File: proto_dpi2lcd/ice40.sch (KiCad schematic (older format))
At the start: 42 parts, among them J101 Conn_02x05_Odd_Even, J6 Conn_01x40_MountingPin, U1 ASDMB-xxxMHz, U102 iCE40HX1K-CB132, U103 W25Q32JVSS, U104 TLV71312PDBV, U105 TLV71325PDBV

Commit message: Work in progress
- Schematic of 12V to 3,3V BUCK
 - pin allocation from RPi header to FPGA
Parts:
- removed C109, C112, C113: 100n, Capacitor_SMD:C_0603_1608Metric, symbol ice40-rescue:C_Small-Device
- removed U104: TLV71312PDBV, Package_TO_SOT_SMD:SOT-23-5, symbol ice40-rescue:TLV71312PDBV-Regulator_Linear
- removed U105: TLV71325PDBV, Package_TO_SOT_SMD:SOT-23-5, symbol ice40-rescue:TLV71325PDBV-Regulator_Linear
- added J102: Raspberry_Pi_2_3, Connector_IDC:IDC-Header_2x20_P2.54mm_Vertical, symbol Connector:Raspberry_Pi_2_3
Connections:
- net labels added: B0, B1, B2, B3, B4, B5, B6, B7, CLK, DEN, G0, G1, G2, G3, G4, G5, G6, G7, H_SYNC, R0, R1, R2, R3, R4, R5, R6, R7, V_SYNC
- net labels removed: 24, 25, 26, 27, 28, 29, 30, 31, 32, 33, 34, 35, 36, 37, 38, 39, 40, 41, 42, 43
- wire segments 281 -> 316
- no-connect marks 15 -> 27
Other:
- moved on the sheet: C117, C118, C119, C120, C121, C122, C123, U102B, U102C, U102D

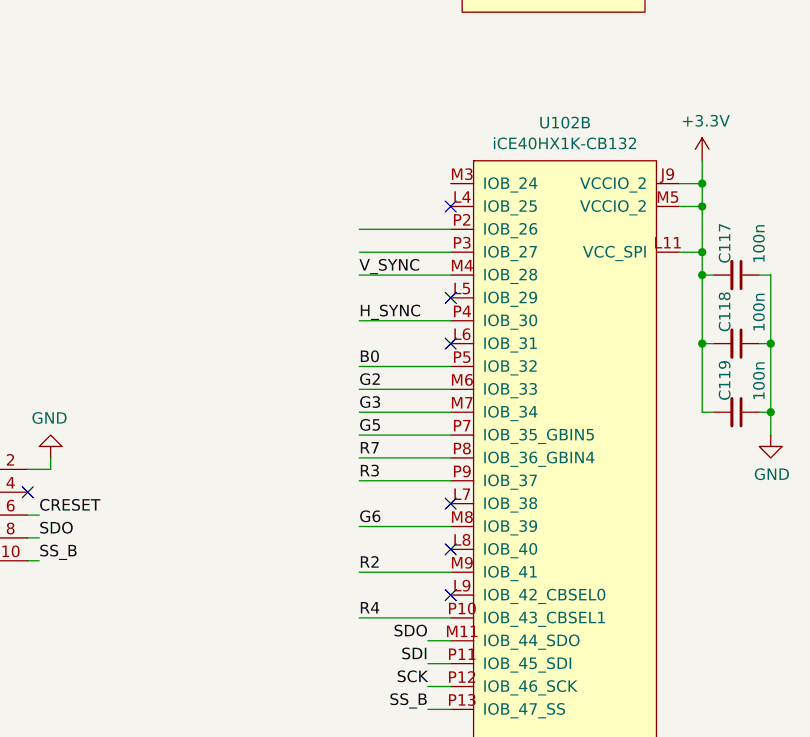
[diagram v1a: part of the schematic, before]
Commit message: Fanout of DPI
(Display Parallel Interface)
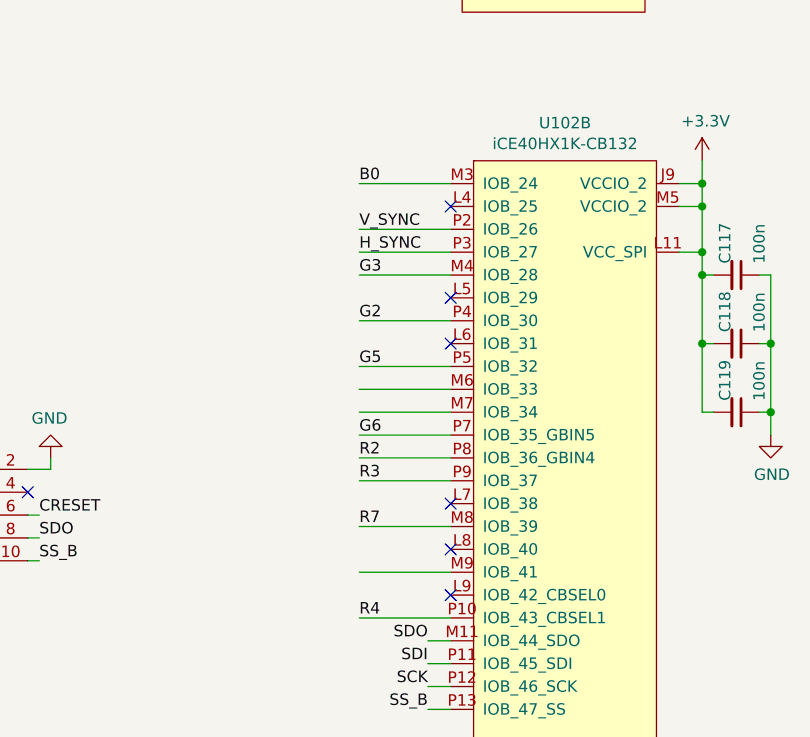
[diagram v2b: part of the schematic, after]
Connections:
- wire segments 316 -> 317
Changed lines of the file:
@@
 Text Label 12200 2650 0    50   ~ 0
 G0
-Text Label 12200 5400 0    50   ~ 0
+Text Label 12200 5100 0    50   ~ 0
 G2
-Text Label 12200 5500 0    50   ~ 0
+Text Label 12200 4900 0    50   ~ 0
 G3
 Text Label 12200 2950 0    50   ~ 0
 G4
+Text Label 12200 5300 0    50   ~ 0
+G5
 Text Label 12200 5600 0    50   ~ 0
-G5
-Text Label 12200 6000 0    50   ~ 0
 G6
 Text Label 12200 2850 0    50   ~ 0
@@
 Text Label 12200 3350 0    50   ~ 0
 R1
-Text Label 12200 6200 0    50   ~ 0
+Text Label 12200 5700 0    50   ~ 0
 R2
 Text Label 12200 5800 0    50   ~ 0
@@
 Text Label 12200 3150 0    50   ~ 0
 R6
-Text Label 12200 5700 0    50   ~ 0
+Text Label 12200 6000 0    50   ~ 0
 R7
-Text Label 12200 5300 0    50   ~ 0
+Text Label 12200 4500 0    50   ~ 0
 B0
 Text Label 12200 2250 0    50   ~ 0
@@
 Wire Wire Line
 	12200 5700 12600 5700
-Text Label 12200 5100 0    50   ~ 0
+Text Label 12200 4800 0    50   ~ 0
 H_SYNC
-Text Label 12200 4900 0    50   ~ 0
+Text Label 12200 4700 0    50   ~ 0
 V_SYNC
 Text Label 12200 2050 0    50   ~ 0
@@
 Wire Wire Line
 	12200 5400 12600 5400
+Wire Wire Line
+	12200 4500 12600 4500
 $EndSCHEMATC

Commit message: Progressing
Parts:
- added D102, D103: Green, Diode_SMD:D_0805_2012Metric, symbol Device:LED
- added R114, R115: 200R, Resistor_SMD:R_0603_1608Metric, symbol Device:R
- added R116, R117: 10k, Resistor_SMD:R_0603_1608Metric, symbol Device:R
- added SW101: SW1, Button_Switch_THT:SW_PUSH_6mm_H4.3mm, symbol Switch:SW_Push
- added SW102: SW2, Button_Switch_THT:SW_PUSH_6mm_H4.3mm, symbol Switch:SW_Push
- C104: renamed from C106; footprint Capacitor_SMD:C_0603_1608Metric -> Capacitor_SMD:C_0402_1005Metric
- C106: renamed from C107; footprint Capacitor_SMD:C_0603_1608Metric -> Capacitor_SMD:C_0402_1005Metric
- C107: renamed from C108; footprint Capacitor_SMD:C_0603_1608Metric -> Capacitor_SMD:C_0402_1005Metric
- C108: renamed from C110; footprint Capacitor_SMD:C_0603_1608Metric -> Capacitor_SMD:C_0402_1005Metric
- C109: renamed from C111; footprint Capacitor_SMD:C_0603_1608Metric -> Capacitor_SMD:C_0402_1005Metric
- U103: renamed from U1; value ASDMB-xxxMHz -> 520-2520MVLC-400BNTR
- renumbered C114 to C101, C104 to C102, C115 to C103, C116 to C105, C103 to C110, C1 to C111, C120 to C112, C121 to C113, C117 to C114, C118 to C115, C119 to C116, C122 to C117, C123 to C118, D1 to D101, J6 to J101, J101 to J103, R105 to R102, R106 to R103, R102 to R104, R110 to R105, R108 to R106, R1 to R107, R2 to R108, R3 to R109, R4 to R110, R5 to R111, R103 to R112, R6 to R113, U102 to U101, U103 to U102
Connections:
- net labels added: LED1, LED2, SW1, SW2
- wire segments 317 -> 326
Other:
- moved on the sheet: R107, R108

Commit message: Progress
Sheets work
 - almost all J101 singals connected with FPGA
 - Bank IOT connected to +2V5
 - bus added between J101 and FPGA
 - general sheet cleanup
 - LEDs and SWs connected to FPGA

PCB work:
 - J101 aligned
 - push buttons and LEDs aligned
 - more fanout to the FPGA

And some other things for sure.
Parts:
- removed J101: Conn_01x40_MountingPin, Connector_FFC-FPC:Hirose_FH12-40S-0.5SH_1x40-1MP_P0.50mm_Horizontal, symbol Connector_Generic_MountingPin:Conn_01x40_MountingPin
- removed R102, R103, R105, R106: 100R 1%, Resistor_SMD:R_0402_1005Metric, symbol ice40-rescue:R_Small-Device
- added H101, H102: MountingHole_Pad, MountingHole:MountingHole_3.2mm_M3_Pad_Via, symbol Mechanical:MountingHole_Pad
- added J101: TFT_LCD_MODULE, Connector_IDC:IDC-Header_2x10_P2.54mm_Vertical, symbol Connector_Generic:Conn_02x10_Odd_Even
- added R102: NM, Resistor_SMD:R_0603_1608Metric, symbol Device:R_Small
- added R103: 22R, Resistor_SMD:R_0603_1608Metric, symbol Device:R_Small
- R114, R115: value 200R -> 470R
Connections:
- net labels added: DPS, RSV, RXout0_N, RXout0_P, RXout1_N, RXout1_P, RXout2_N, RXout2_P, RXout3_N, RXout3_P, RxoutC_N, RxoutC_P, SEL68, lcd_VCC
- net labels removed: CLK_EDID, DATA_EDID, GNDPWR, LED_EN, LED_PWM, LED_VCCS, VCCS, VEDID
- wire segments 326 -> 327
- no-connect marks 27 -> 13
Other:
- note added: "CLOCK: \n50Ω Single Ended \nto GBIN5"
- note added: "DPI Routing with \ncontrolled impedance\n\nSingle ended \nsingals with 50Ω:\n - R[0..7]\n - G[0..7]\n - B[0..7]\n - CLK\n - V_SYNC\n - H_SYNC\n\nWithout controlled \nimpedance:\n - DEN\n"
- note added: "LED1 and LED2 to IOB bank"
- note added: "SW1 and SW2 to IOT bank"
- note removed: "12V (5-21V)"
- note removed: "3V3"
- note removed: "LED_GND"
- note removed: "NOTE: Pin numbering swapped compared to display datasheet"
- moved on the sheet: C101, C103, C105, C110, C111, C112, C113, C114, C115, C116, C117, C118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

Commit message: Work in progress
- Added BUCK for 12V->5V but inductors are TBD
 - Progress to the layout
 - some pin swapping has been done
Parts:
- added C119: 22u/25V, Capacitor_SMD:C_1210_3225Metric, symbol Device:C
- added FB101: Ferrite_Bead_Small, Inductor_SMD:L_1210_3225Metric_Pad1.42x2.65mm_HandSolder, symbol Device:Ferrite_Bead_Small
- added J104: LCD_BACKLIGHT, Connector_PinHeader_2.54mm:PinHeader_1x05_P2.54mm_Vertical, symbol Connector_Generic:Conn_01x05
- C101, C103, C105: footprint Capacitor_SMD:C_0603_1608Metric -> Capacitor_SMD:C_0402_1005Metric
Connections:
- net labels added: +12V, BL_ADJ, BL_EN
- wire segments 327 -> 339
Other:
- moved on the sheet: H101, H102, R102

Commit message: 1st routing of the rpi connector
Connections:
- net B0: now also U101.M4 (IOB_28); no longer U101.M3 (IOB_24)
- net G2: now also U101.P3 (IOB_27); no longer U101.P4 (IOB_30)
- net G3: now also U101.P4 (IOB_30); no longer U101.M4 (IOB_28)
- net G5: now also U101.M7 (IOB_34); no longer U101.P5 (IOB_32)
- net G6: now also U101.P5 (IOB_32); no longer U101.M7 (IOB_34)
- net H_SYNC: now also U101.M3 (IOB_24); no longer U101.P3 (IOB_27)
- net R2: now also U101.P9 (IOB_37); no longer U101.P8 (IOB_36_GBIN4)
- net R3: now also U101.P8 (IOB_36_GBIN4); no longer U101.P9 (IOB_37)
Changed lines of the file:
@@
 U 1 1 618A6A59
 P 11000 2600
-F 0 "J102" H 11000 4081 50  0000 C CNN
-F 1 "Raspberry_Pi_2_3" H 11000 3990 50  0000 C CNN
+F 0 "J102" H 11450 1300 50  0000 C CNN
+F 1 "Raspberry_Pi_2_3" H 11000 1100 50  0000 C CNN
 F 2 "Connector_IDC:IDC-Header_2x20_P2.54mm_Vertical" H 11000 2600 50  0001 C CNN
 F 3 "https://www.raspberrypi.org/documentation/hardware/raspberrypi/schematics/rpi_SCH_3bplus_1p0_reduced.pdf" H 11000 2600 50  0001 C CNN
@@
 Text Label 13100 2600 0    50   ~ 0
 G0
+Text Label 13100 4950 0    50   ~ 0
+G2
 Text Label 13100 5250 0    50   ~ 0
-G2
-Text Label 13100 5050 0    50   ~ 0
 G3
 Text Label 13100 3000 0    50   ~ 0
 G4
+Text Label 13100 5650 0    50   ~ 0
+G5
 Text Label 13100 5450 0    50   ~ 0
-G5
-Text Label 13100 5650 0    50   ~ 0
 G6
 Text Label 13100 3100 0    50   ~ 0
@@
 Text Label 13100 3500 0    50   ~ 0
 R1
+Text Label 13100 5950 0    50   ~ 0
+R2
 Text Label 13100 5850 0    50   ~ 0
-R2
-Text Label 13100 5950 0    50   ~ 0
 R3
 Text Label 13100 6550 0    50   ~ 0
@@
 Text Label 13100 6150 0    50   ~ 0
 R7
-Text Label 13100 4650 0    50   ~ 0
+Text Label 13100 5050 0    50   ~ 0
 B0
 Text Label 13100 2700 0    50   ~ 0
@@
 Wire Wire Line
 	13100 5850 13600 5850
-Text Label 13100 4950 0    50   ~ 0
+Text Label 13100 4650 0    50   ~ 0
 H_SYNC
 Text Label 13100 4850 0    50   ~ 0
@@
 	8250 1000 9250 1000
 Wire Notes Line
-	9250 1000 9250 2400
+	9250 1000 9250 2500
 Wire Notes Line
-	9250 2400 8250 2400
+	9250 2500 8250 2500
 Wire Notes Line
-	8250 2400 8250 1000
+	8250 2500 8250 1000
 Text Notes 9700 9350 0    50   Italic 0
 SW1 and SW2 to IOT bank
